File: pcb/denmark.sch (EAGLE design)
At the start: 81 parts, among them IC1 74AHC1G32DBV, IC2 REG1117, U2 MB85RCSOIC8, X1 22-23-2021, X2 22-23-2031, X3 22-23-2051, X4 22-23-2021

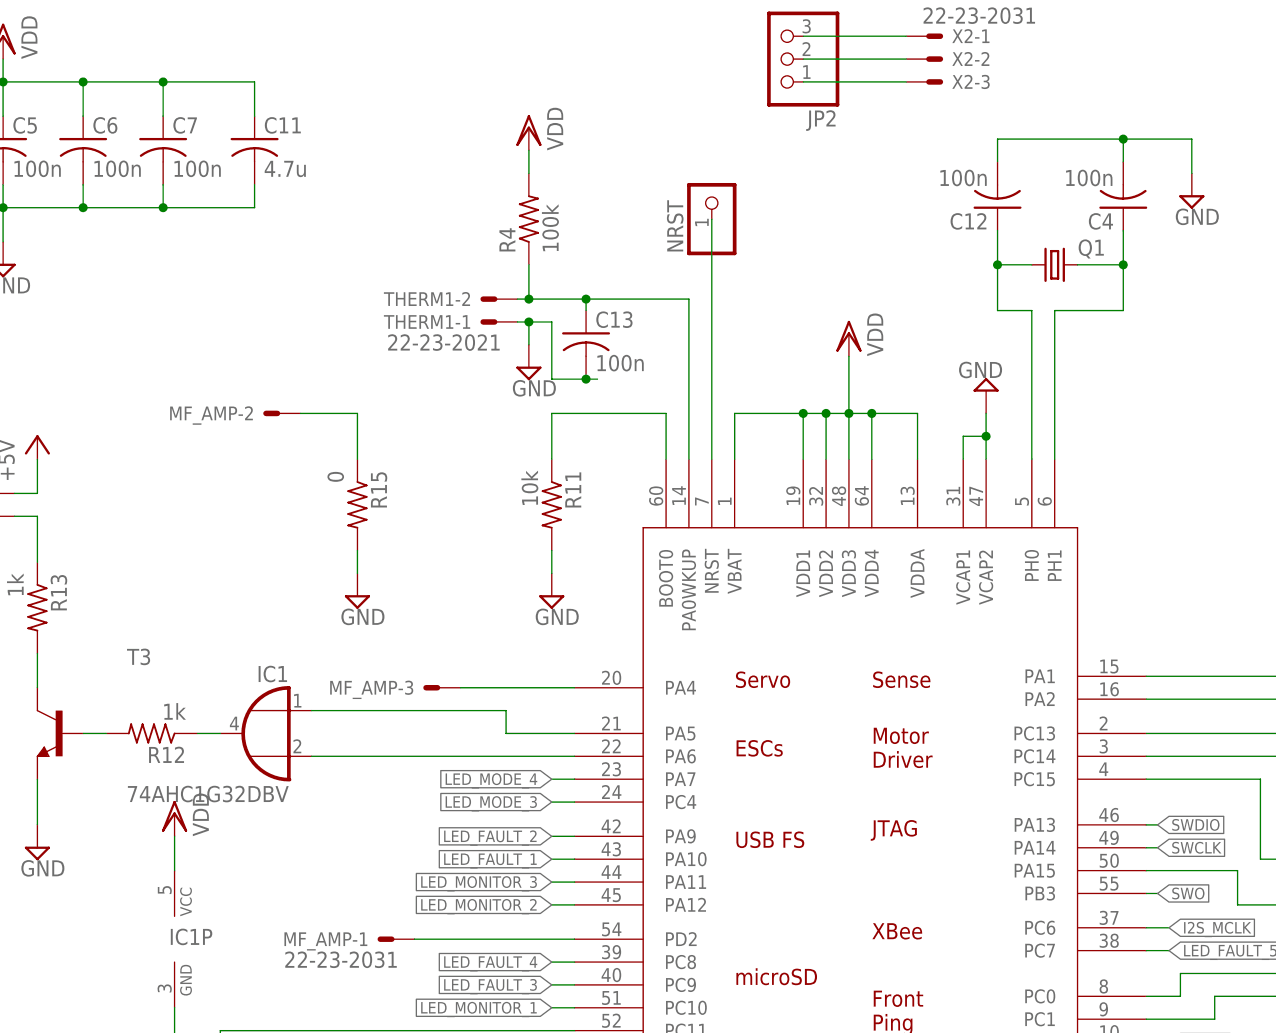
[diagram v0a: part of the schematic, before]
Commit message: Update MCU footprint and add BOM
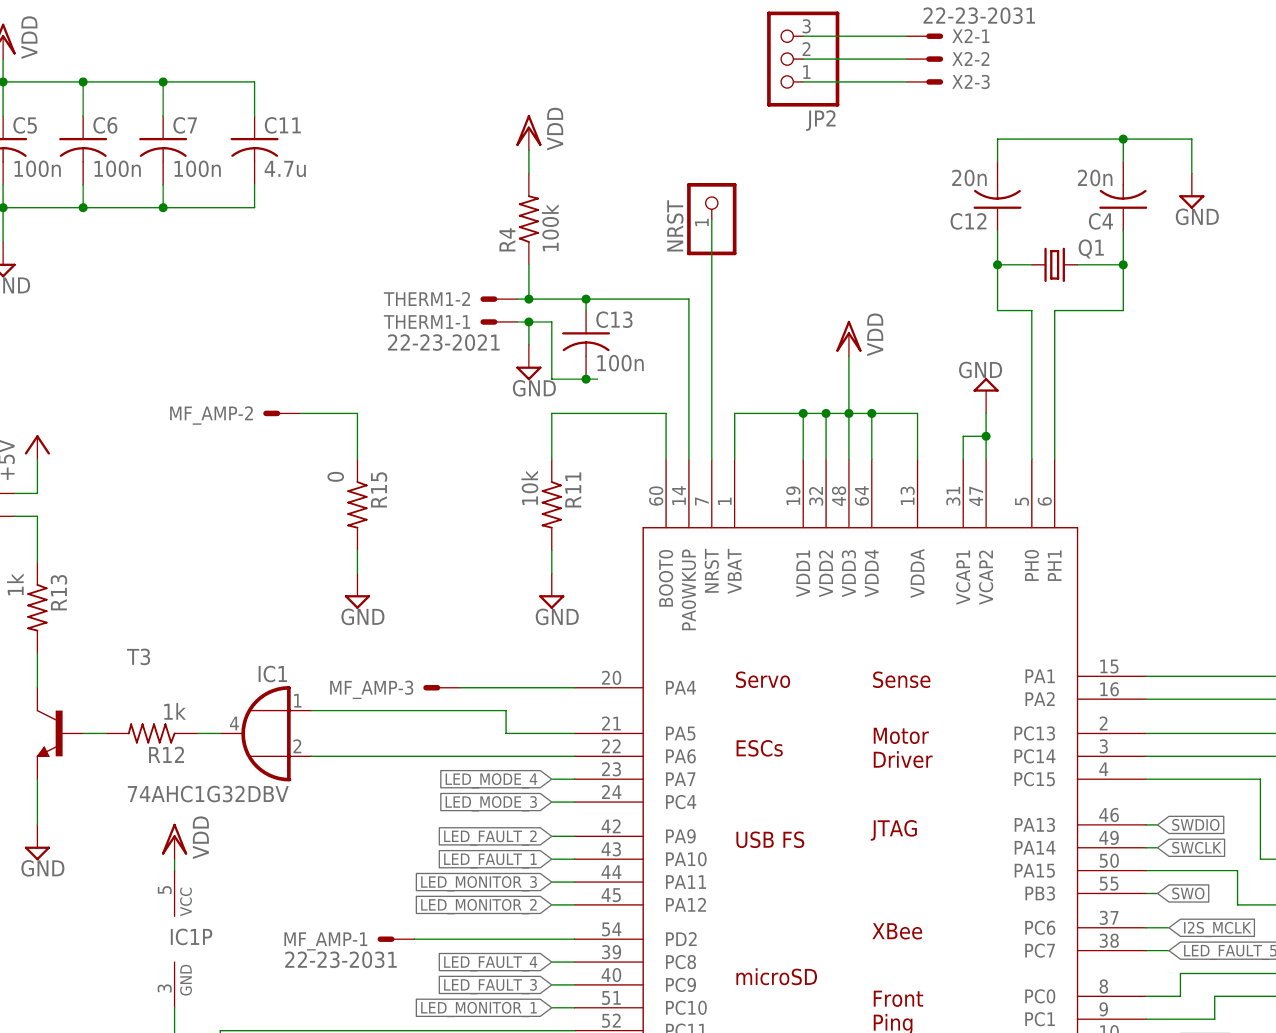
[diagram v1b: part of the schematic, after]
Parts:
- C12, C4: value 100n -> 20n
- U$1: value STM32F4R_64PIN_FOXCAR -> STM32F4_10X10_LQFP64; device stm32f4:STM32F4R_64PIN_FOXCAR -> stm32f4:STM32F4_10X10_LQFP64

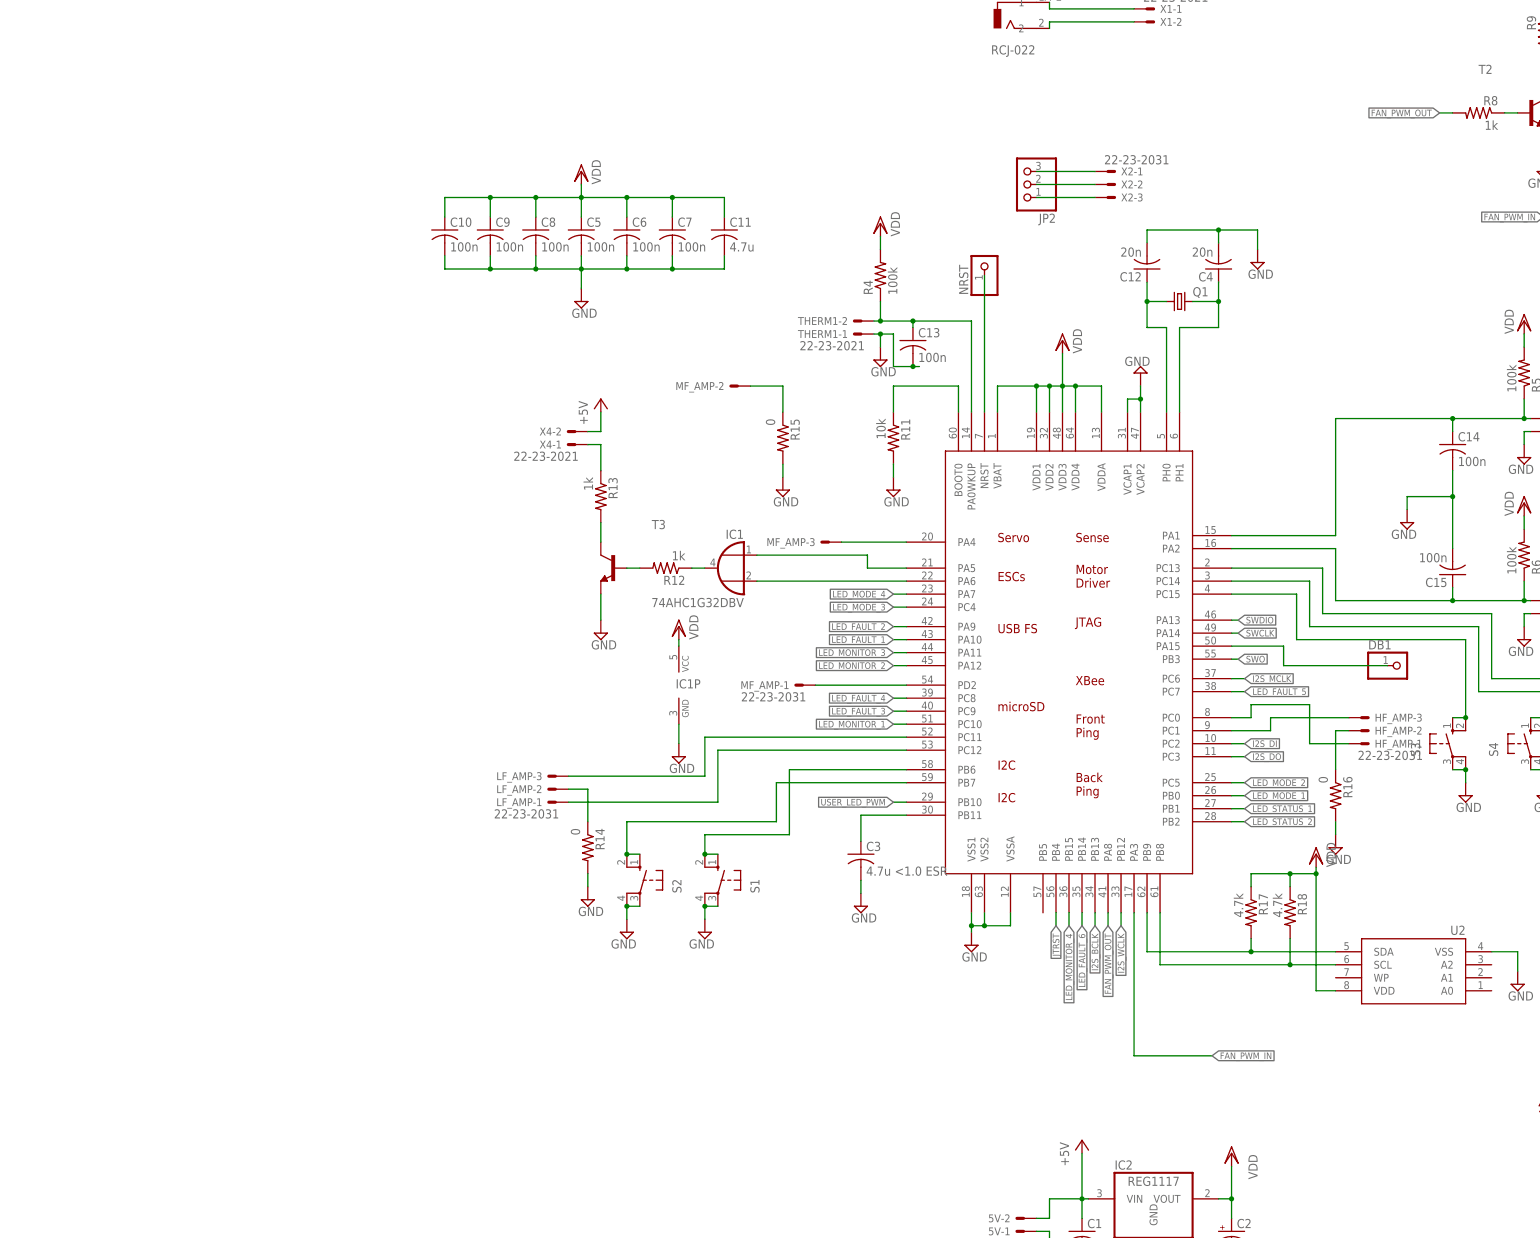
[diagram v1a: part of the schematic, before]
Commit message: Update BOM and PCB to incorporate reworks
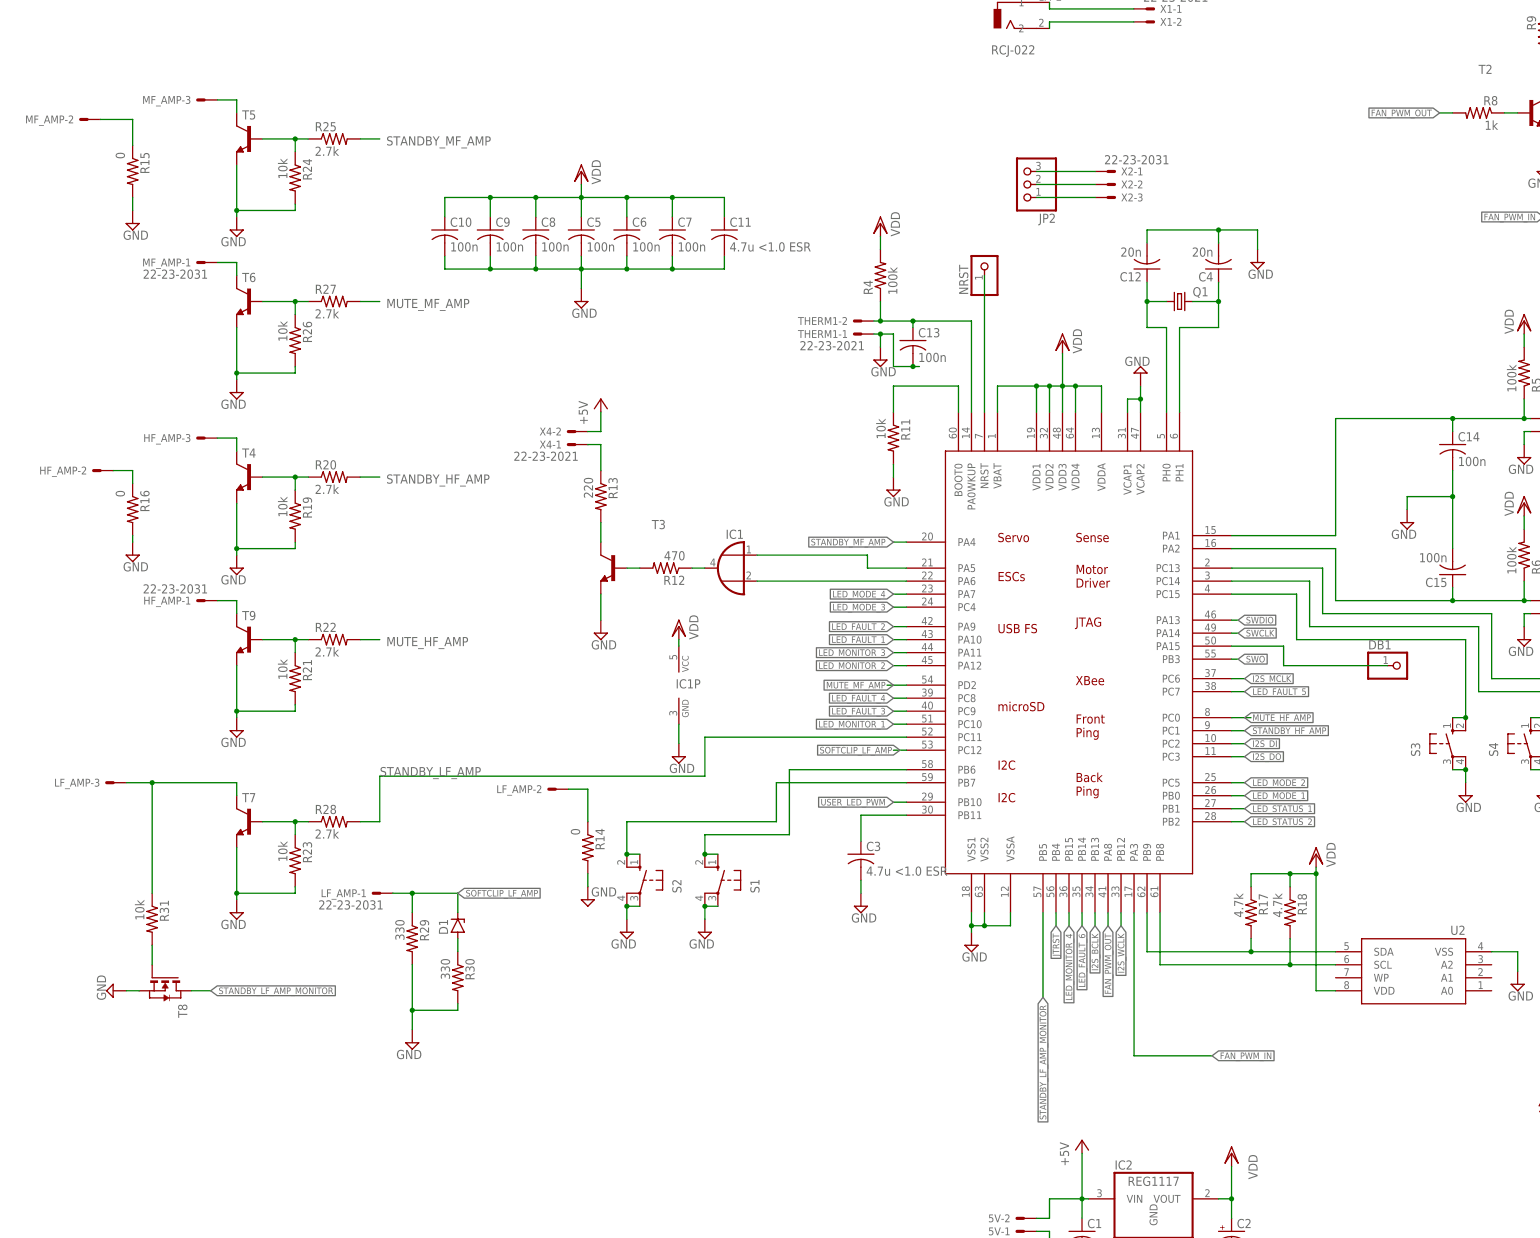
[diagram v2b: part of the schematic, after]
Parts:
- added D1: (no value), diode:ZENER-DIODESOD80C
- added R19, R21, R23, R24, R26, R31: 10k, rcl:R-US_R0603
- added R20, R22, R25, R27, R28: 2.7k, rcl:R-US_R0603
- added R29, R30: 330, rcl:R-US_R0603
- added T4, T5, T6, T7, T9: (no value), transistor:MMBT3904LT1-NPN-SOT23-BEC
- added T8: (no value), zetex:NMOSSOT23
- C11: value 4.7u -> 4.7u <1.0 ESR; device rcl:C-USC0805 -> rcl:C-USC1206
- R12: value 1k -> 470
- R13: value 1k -> 220
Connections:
- new net N$18: HF_AMP-3.S, T4.C
- new net N$19: R19.1, R20.1, T4.B
- new net N$20: HF_AMP-1.S, T9.C
- new net N$21: R21.1, R22.1, T9.B
- new net N$22: LF_AMP-3.S, R31.1, T7.C
- new net N$23: MF_AMP-3.S, T5.C
- new net N$24: R24.1, R25.1, T5.B
- new net N$27: MF_AMP-1.S, T6.C
- new net N$28: R26.1, R27.1, T6.B
- new net N$29: R23.1, R28.1, T7.B
- new net N$35: R31.2, T8.G
- new net N$41: D1.A, R30.1
- new net STANDBY_LF_AMP_MONITOR: T8.D, U$1.PB5
- net GND: now also R19.2, R21.2, R23.2, R24.2, R26.2, R29.2, R30.2, T4.E, T5.E, T6.E, T7.E, T8.S, T9.E
- net MUTE_HF_AMP: now also R22.2; no longer HF_AMP-1.S
- net MUTE_MF_AMP: now also R27.2; no longer MF_AMP-1.S
- net SOFTCLIP_LF_AMP: now also D1.C, R29.1
- net STANDBY_HF_AMP: now also R20.2; no longer HF_AMP-3.S
- net STANDBY_LF_AMP: now also R28.2; no longer LF_AMP-3.S
- net STANDBY_MF_AMP: now also R25.2; no longer MF_AMP-3.S
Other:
- moved on the sheet: HF_AMP-1, HF_AMP-2, HF_AMP-3, LF_AMP-1, LF_AMP-3, MF_AMP-1, MF_AMP-2, MF_AMP-3, R15, R16

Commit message: Cleanup Schematic
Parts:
- C12, C4: value 20n -> 20p
- Q1: value (none) -> 8.0 MHz
- R1, R2: value (none) -> 330
- R9: value NS -> 2.2k
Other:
- note added: "(5V-1.2V-0.3V)/220Ohm = 16mA"
- note added: "4-Wire 5V PWM Fan Interface"
- note added: "Amp Interfaces to 12V logic"
- note added: "Back panel connectors"
- note added: "I2S Full Duplex"
- note added: "Infrared emitter"
- note added: "LED Array"
- note added: "Power and Decoupling"
- note added: "Programming header"
- note added: "RCA Pass-through"
- note added: "TOSLINK Pass-through"
- note added: "USB Pass-through"
